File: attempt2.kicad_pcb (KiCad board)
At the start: 4 copper layers, 71.5 x 54.4 mm, 60 parts, among them J3 Conn_02x05_Pin, J4 USB_C_Receptacle_USB2.0_14P, J5 SIM_Card, SW1 SW_Push, SW4 SW_Push, U3 MCP73831T-2ACI_OT, U4 NRF9151-LACA-R7, U5 MAX2686LEWS_, U6 TPD3F303DPVR, U7 CP2102N-A02-GQFN24R

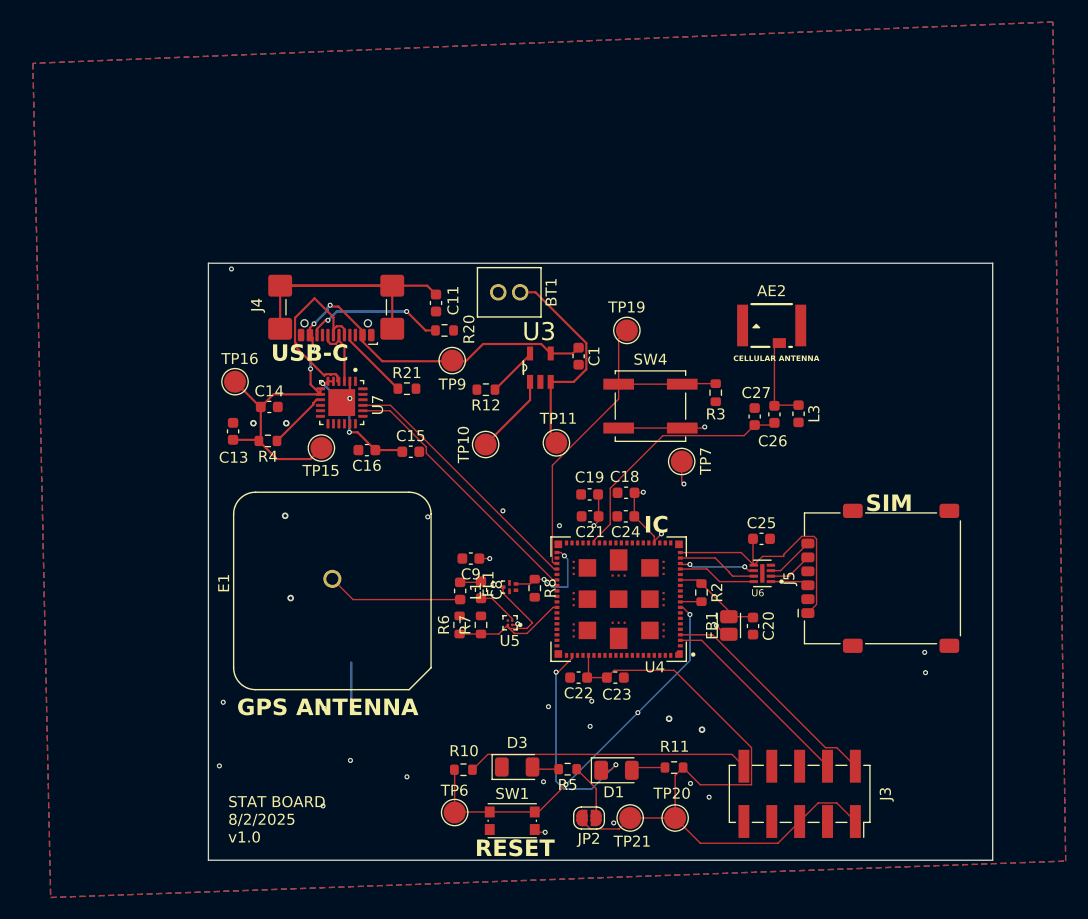
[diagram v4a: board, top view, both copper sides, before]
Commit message: increased thickness of antenna and power lines. cleaned up silkscreen a little more. added missing capacitor and ferrite bead values. deleted a few useless testpoints
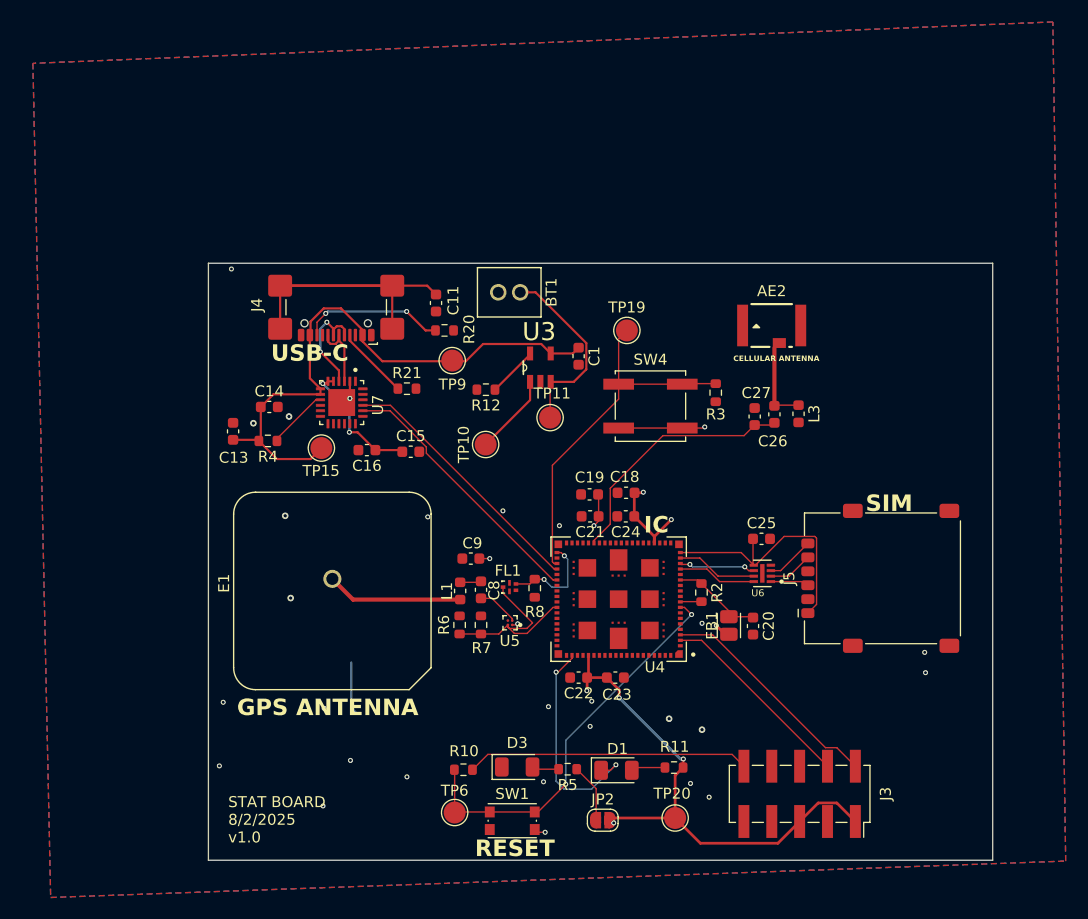
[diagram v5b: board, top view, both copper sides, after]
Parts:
- removed TP16, TP21, TP7: TestPoint, TestPoint:TestPoint_Pad_D2.0mm
- moved TP11 2.37 mm to (132.2, 101.0)
- moved JP2 1.27 mm to (136.9, 137.8), turned to 0 degrees
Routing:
- net +3V8: track 107.6 -> 87.2 mm, vias 8 -> 10
- net DN: track 17.2 -> 10.0 mm, vias 0 -> 2
- net VBUS: track 58.1 -> 54.1 mm, vias 4 -> 0
- net Net-(U4A-~{RESET}): track 36.4 -> 36.6 mm, vias 3 -> 2
- net GND: vias 27 -> 28

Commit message: small things
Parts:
- C18, C21: value C -> 1u
- C19: value C -> 47u
- C20: value C -> 10u
- C24: value C -> 4.7u
- FB1: value FerriteBead -> 22R/100MHz
- moved R8 3.80 mm to (127.0, 116.0), turned to 180 degrees
- moved C9 2.54 mm to (123.5, 116.0)
- moved C8 2.34 mm to (126.5, 119.0), turned to 0 degrees
- moved L1 2.20 mm to (123.5, 119.0), turned to 180 degrees
- moved U5 1.80 mm to (130.3, 119.8)
- moved FL1 1.55 mm to (130.0, 116.5), turned to 90 degrees
- moved R7 1.23 mm to (126.5, 121.0), turned to 0 degrees
- moved R6 1.12 mm to (123.5, 121.0), turned to 180 degrees
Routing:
- net COEX0: track 17.5 -> 12.7 mm
- net GPS: track 8.97 -> 6.12 mm, vias 2 -> 0
- net Net-(U5-RFIN): track 3.79 -> 5.51 mm, vias 0 -> 2
- net +3V8: track 87.2 -> 88.3 mm
- net Net-(E1-Pad1): track 12.4 -> 11.8 mm
- net UART_TX: track 24.4 -> 24.1 mm, vias 0 -> 2
- net USER_BTN: track 33.3 -> 33.0 mm, vias 0 -> 2
- net UART_RX: vias 0 -> 2

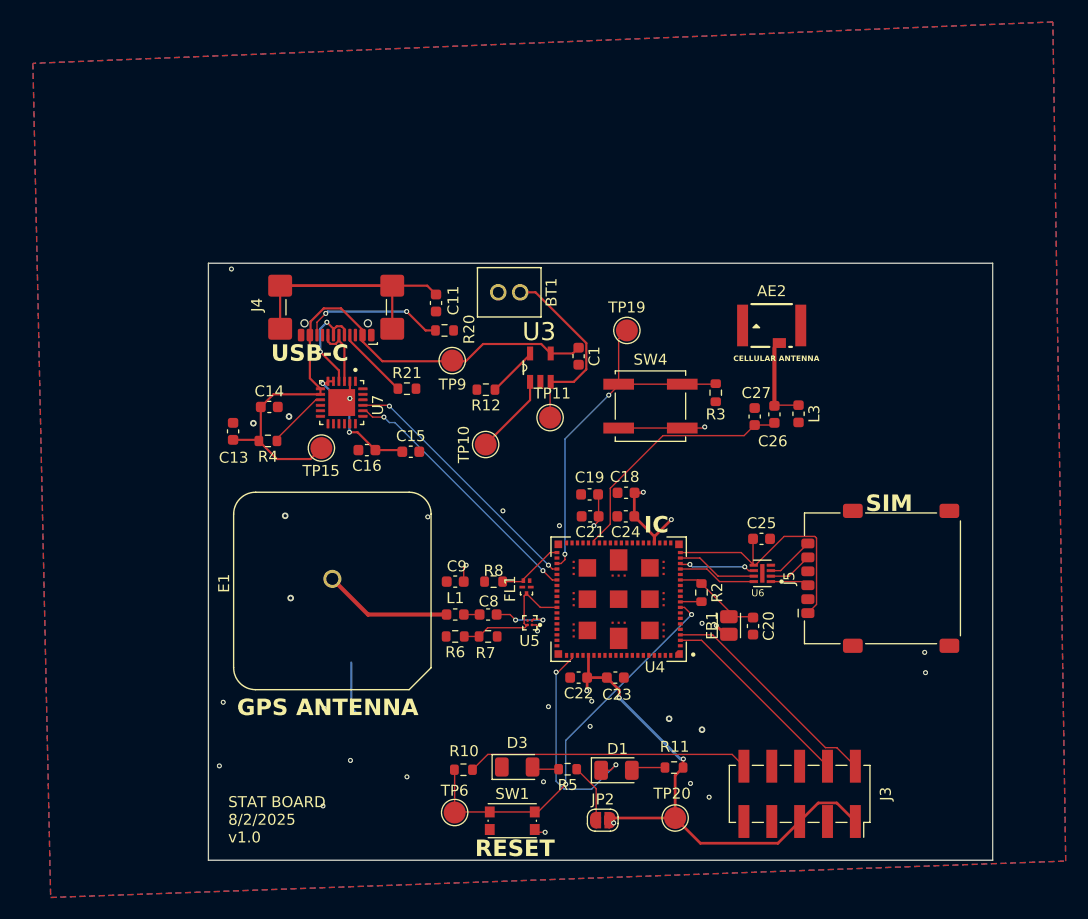
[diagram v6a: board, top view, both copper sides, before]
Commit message: moved antennas to be perpendicular to ic and cleaned silkscreen
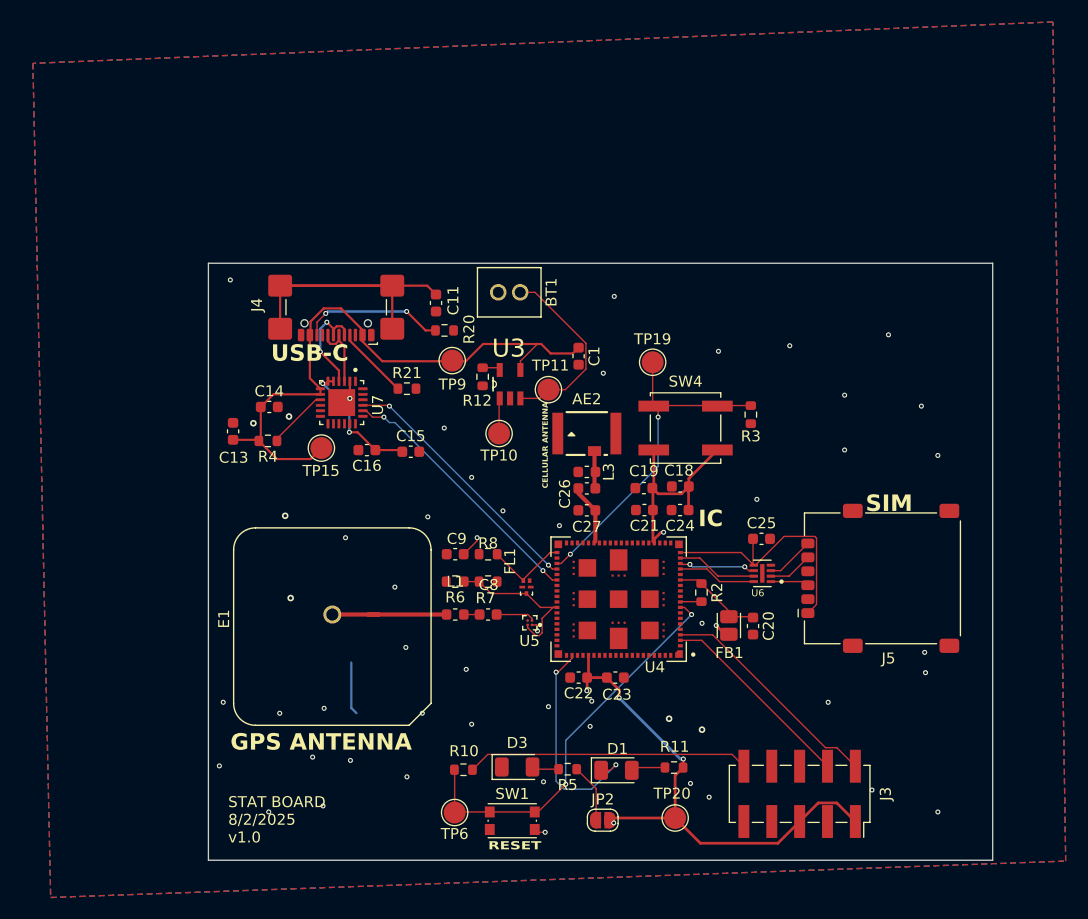
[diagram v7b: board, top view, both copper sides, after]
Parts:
- moved L3 20.0 mm to (135.5, 106.0), turned to 180 degrees
- moved AE2 19.5 mm to (135.5, 102.5)
- moved C26 18.4 mm to (135.5, 107.5), turned to 180 degrees
- moved C27 17.5 mm to (135.5, 109.5), turned to 180 degrees
- moved R6 5.00 mm to (123.5, 116.0)
- moved R7 5.00 mm to (126.5, 116.0)
- moved C18 4.98 mm to (144.0, 107.3)
- moved C19 4.98 mm to (140.7, 107.5)
- moved C21 4.98 mm to (140.8, 109.5)
- moved C24 4.98 mm to (144.0, 109.5)
- moved R3 3.77 mm to (150.4, 100.8)
- moved SW4 3.77 mm to (144.5, 102.0)
- moved TP19 3.73 mm to (141.5, 96.0)
- moved E1 3.25 mm to (112.3, 120.1)
- moved U3 3.15 mm to (128.5, 98.0)
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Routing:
- net Net-(U4A-ANT): track 23.0 -> 5.67 mm
- net Net-(AE2-Pad3): track 8.14 -> 3.43 mm
- net Net-(U3-STAT): track 7.39 -> 3.23 mm
- net Net-(U3-PROG): track 4.73 -> 1.64 mm
- net VBUS: track 54.1 -> 57.1 mm
- net Net-(U5-RFIN): track 5.51 -> 3.56 mm, vias 2 -> 0
- net COEX0: track 12.7 -> 14.5 mm
- net USER_BTN: track 33.0 -> 31.5 mm
- net GPS: track 6.12 -> 7.60 mm
- net +3V8: track 88.3 -> 89.2 mm, vias 10 -> 7
- net GND: vias 28 -> 52

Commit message: i added the flooded ground planes around the gps and cellular antenna
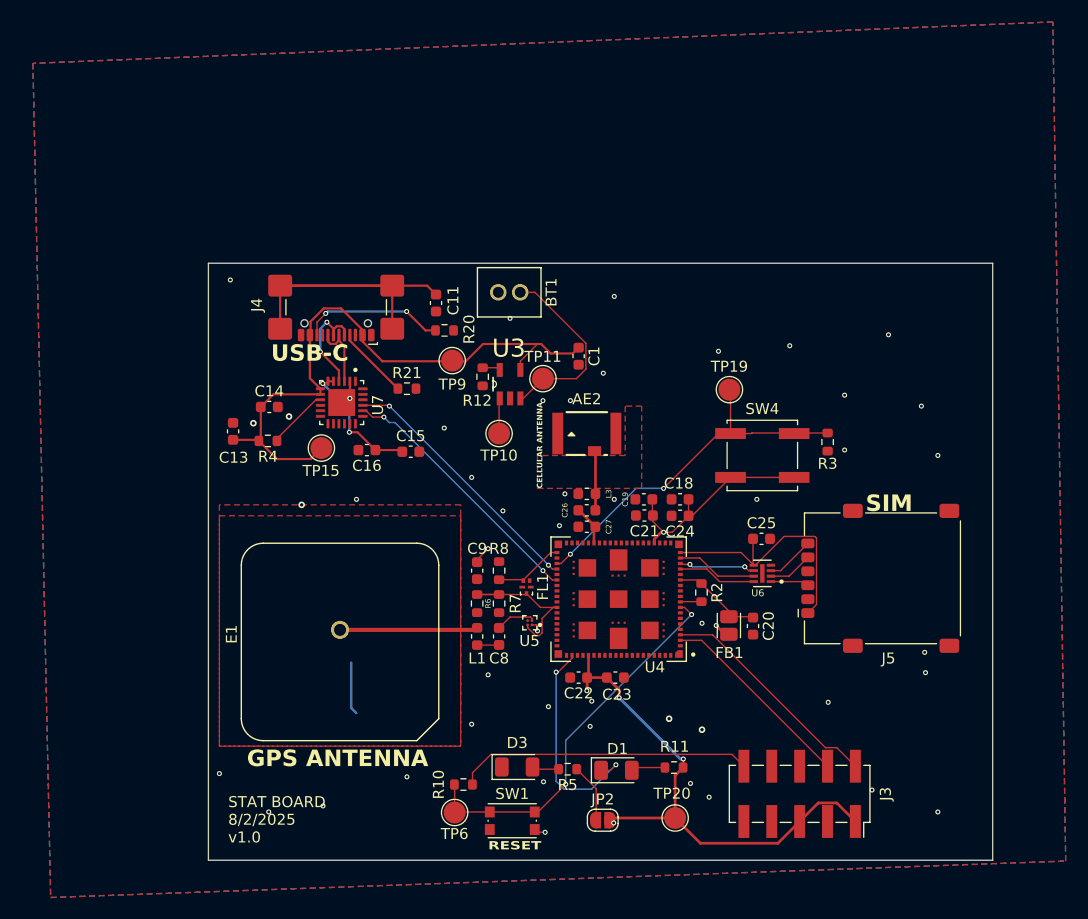
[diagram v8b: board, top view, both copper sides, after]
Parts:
- moved R3 7.43 mm to (157.4, 103.3)
- moved SW4 7.43 mm to (151.5, 104.5)
- moved TP19 7.43 mm to (148.5, 98.5)
- moved L1 2.83 mm to (125.5, 121.0), turned to 90 degrees
- moved R6 2.83 mm to (125.5, 118.0), turned to -90 degrees
- moved C9 2.50 mm to (125.5, 115.0), turned to -90 degrees
- moved C8 2.24 mm to (127.5, 121.0), turned to 90 degrees
- moved R7 2.24 mm to (127.5, 118.0), turned to -90 degrees
- moved C26 2.00 mm to (135.5, 109.5)
- moved L3 2.00 mm to (135.5, 108.0)
- moved R8 1.80 mm to (127.5, 115.0), turned to 90 degrees
- moved E1 1.57 mm to (113.0, 121.5)
- moved C27 1.50 mm to (135.5, 111.0)
- moved R10 1.35 mm to (124.2, 134.5)
- moved C18 1.18 mm to (144.0, 108.5)
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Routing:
- net USER_BTN: track 31.5 -> 33.6 mm
- net Net-(AE2-Pad3): track 3.43 -> 5.44 mm
- net Net-(U4A-ANT): track 5.67 -> 3.70 mm
- net Net-(U4A-~{RESET}): track 36.6 -> 35.3 mm
- net Net-(E1-Pad1): track 11.4 -> 12.6 mm
- net Net-(J3-Pin_10): track 25.8 -> 27.0 mm
- net GPS: track 7.60 -> 6.42 mm
- net Net-(C8-Pad1): track 1.44 -> 2.01 mm
- net GND: vias 52 -> 47
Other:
- board text removed: "IC"
